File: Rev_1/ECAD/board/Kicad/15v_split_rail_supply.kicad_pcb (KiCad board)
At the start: 4 copper layers, 71.1 x 39.4 mm, 90 parts, among them Q1 NPN, Q100 IPP029N15NM6, Q101 NPN, Q102 NPN, Q103 PMOS, Q2 NPN, U1 LM3478MA, U100 LM3478MA, U2 LM358, U3 LM358, U4 SN74AHC1G02DBVR, U5 SN74AHC1G02DBVR

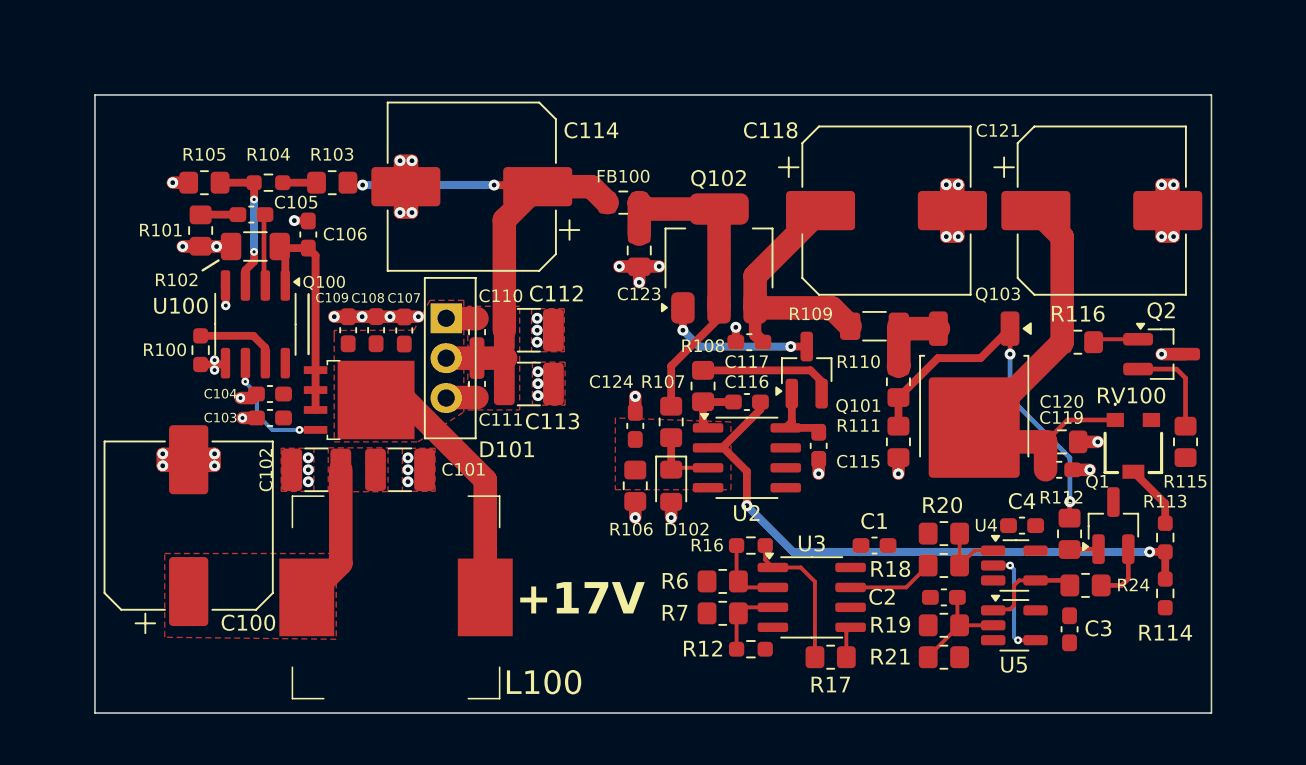
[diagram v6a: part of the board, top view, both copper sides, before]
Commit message: Added inverted buck-boost for -17V rail
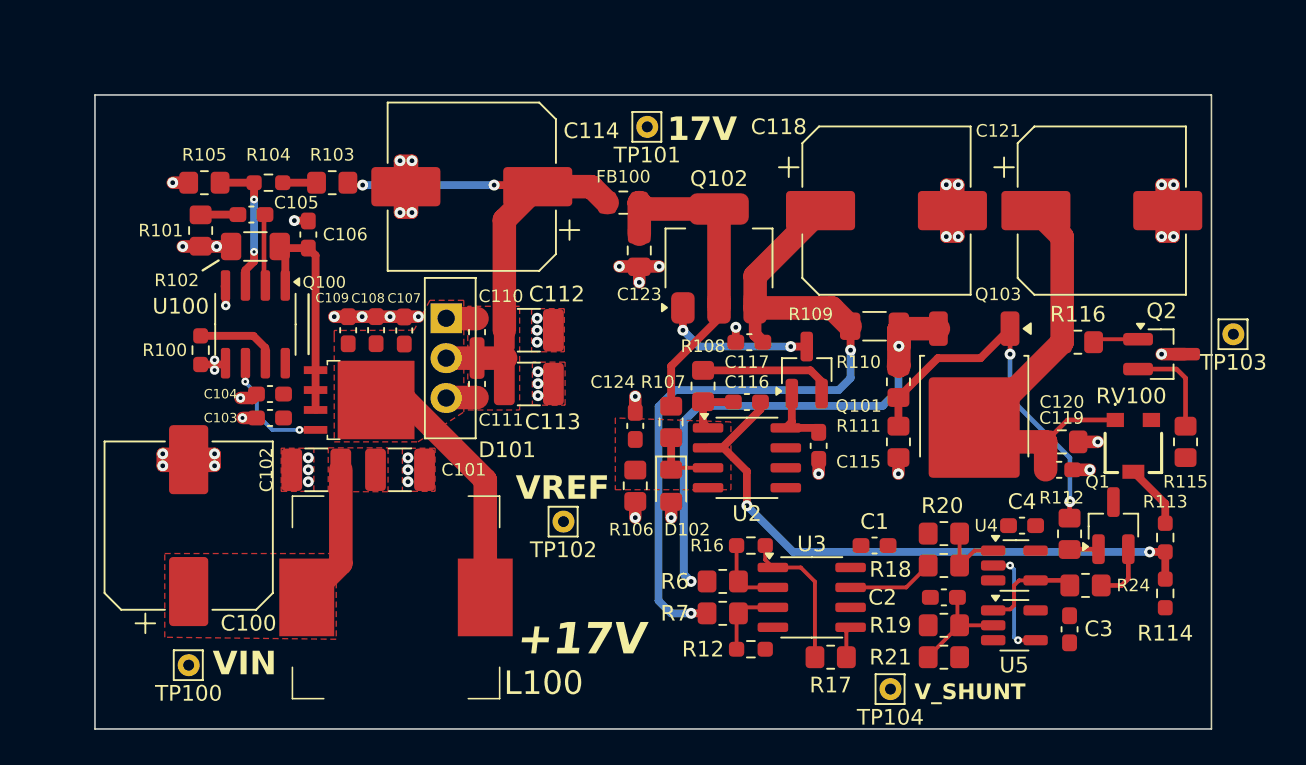
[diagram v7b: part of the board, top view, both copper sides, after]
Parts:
- added TP100: VIN, Connector_Pin:Pin_D0.7mm_L6.5mm_W1.8mm_FlatFork, F.Cu at (119.6, 104.1)
- added TP101: 17V, Connector_Pin:Pin_D0.7mm_L6.5mm_W1.8mm_FlatFork, F.Cu at (148.8, 69.8)
- added TP102: VREF, Connector_Pin:Pin_D0.7mm_L6.5mm_W1.8mm_FlatFork, F.Cu at (143.5, 95.0)
- added TP103: 15V, Connector_Pin:Pin_D0.7mm_L6.5mm_W1.8mm_FlatFork, F.Cu at (186.2, 83.1)
- added TP104: VIN, Connector_Pin:Pin_D0.7mm_L6.5mm_W1.8mm_FlatFork, F.Cu at (164.3, 105.7)
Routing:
- net /+15V DC-DC Converter/SHUNT_IN: track 16.9 -> 48.9 mm, vias 0 -> 2
- net /+15V DC-DC Converter/SHUNT_OUT: track 5.11 -> 33.6 mm, vias 0 -> 2
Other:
- board size 71.1 x 39.4 mm -> 71.1 x 40.4 mm
- board text added: "17V"
- board text added: "VIN"
- board text added: "VREF"
- board text added: "V_SHUNT"

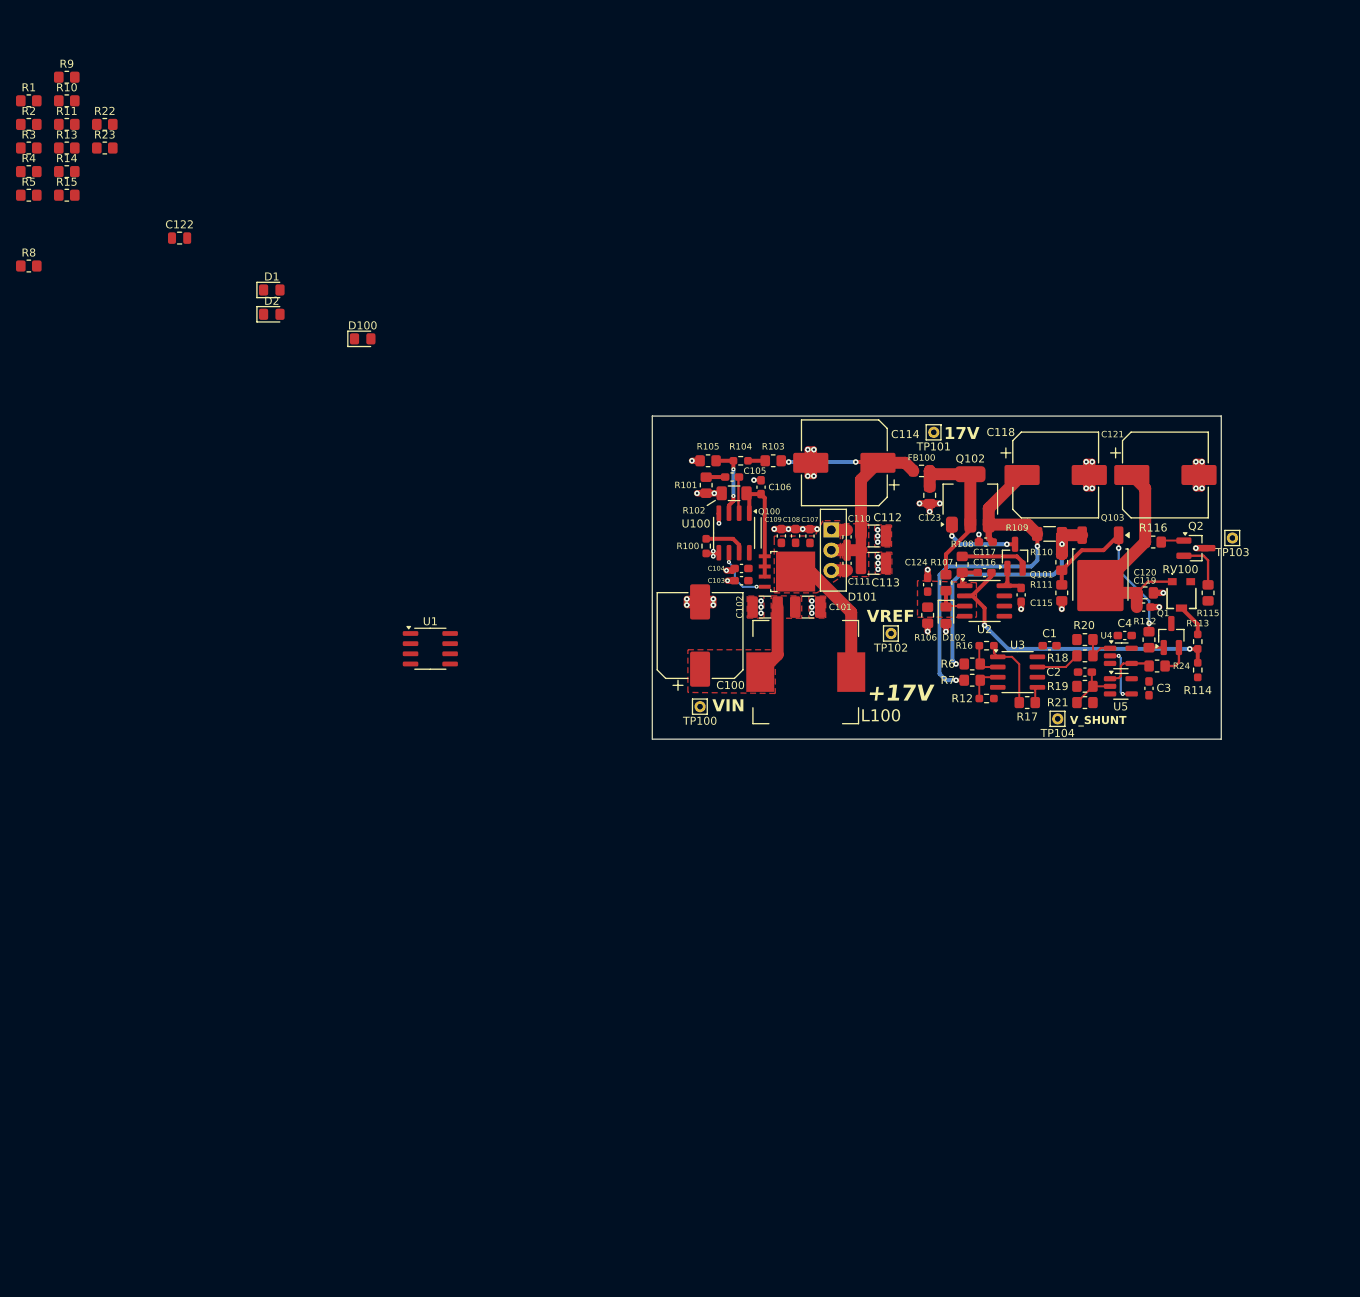
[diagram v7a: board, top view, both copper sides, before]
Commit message: Added Heatsink to Transistors
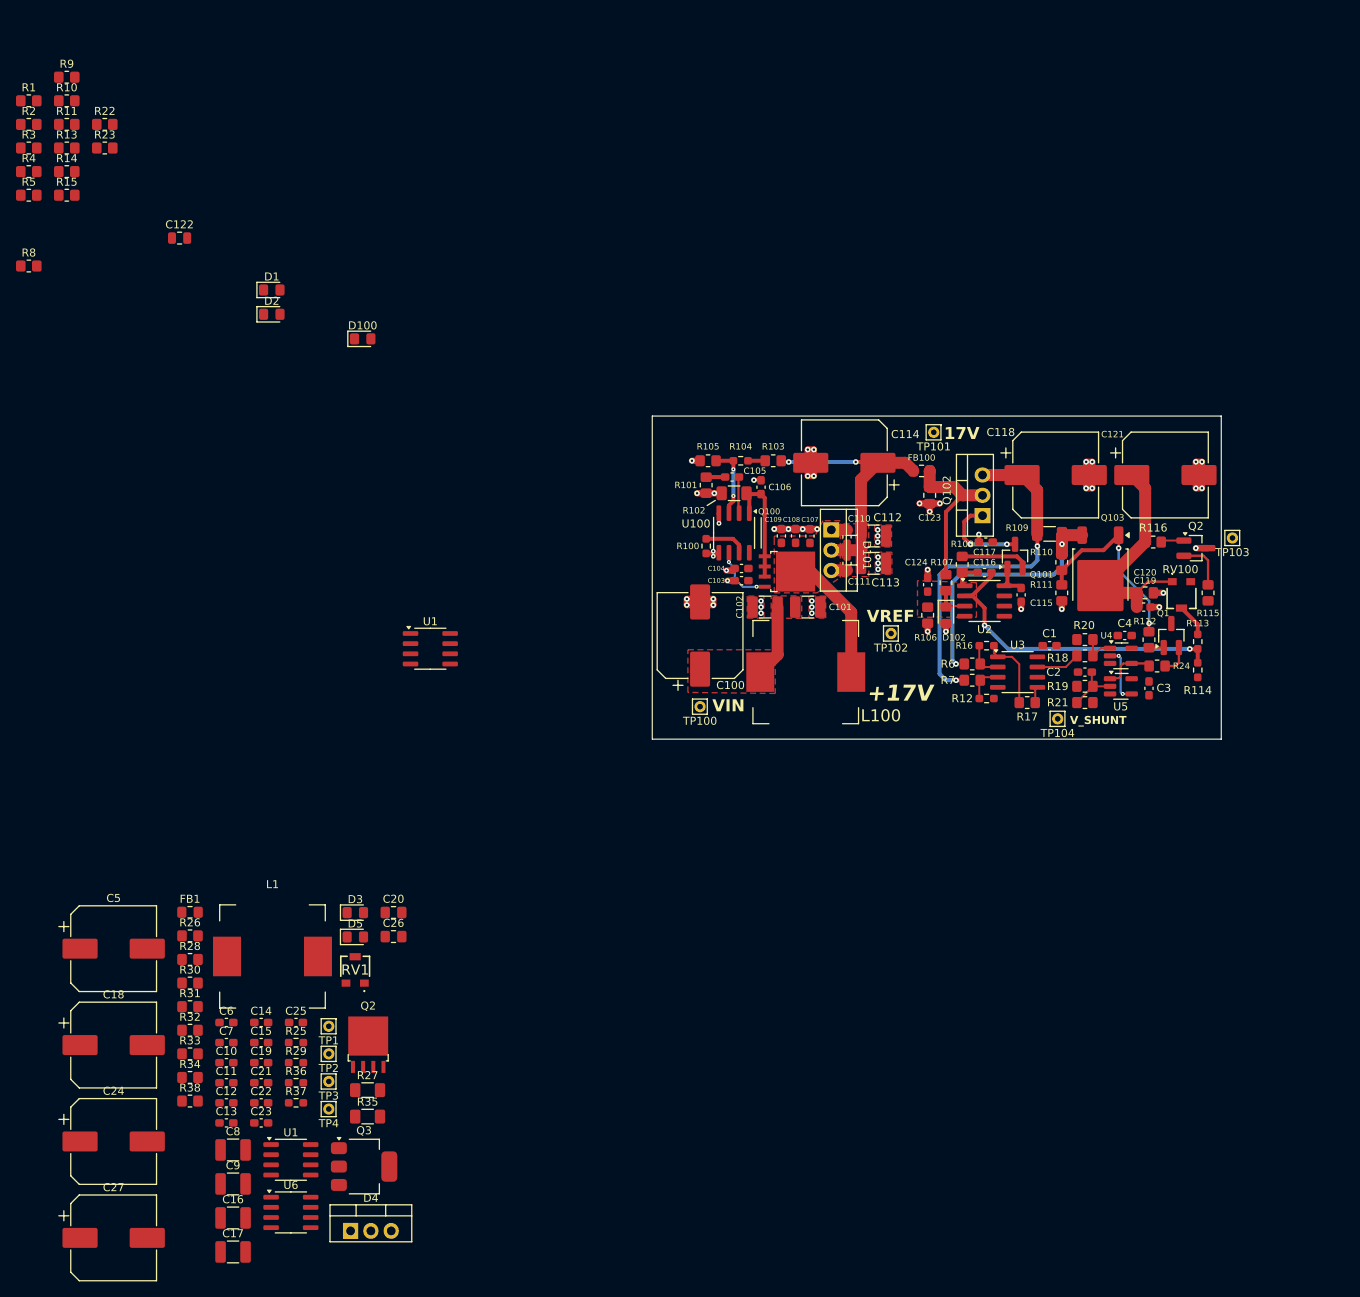
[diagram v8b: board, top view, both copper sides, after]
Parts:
- added C10: 2.2n, Capacitor_SMD:C_0603_1608Metric_Pad1.08x0.95mm_HandSolder, F.Cu at (60.4, 148.6)
- added C11: 100n, Capacitor_SMD:C_0603_1608Metric_Pad1.08x0.95mm_HandSolder, F.Cu at (60.4, 151.2)
- added C12: 100n, Capacitor_SMD:C_0603_1608Metric_Pad1.08x0.95mm_HandSolder, F.Cu at (60.4, 153.7)
- added C13: 220n, Capacitor_SMD:C_0603_1608Metric_Pad1.08x0.95mm_HandSolder, F.Cu at (60.4, 156.2)
- added C14: 1u, Capacitor_SMD:C_0603_1608Metric_Pad1.08x0.95mm_HandSolder, F.Cu at (64.8, 143.6)
- added C15: 100n, Capacitor_SMD:C_0603_1608Metric_Pad1.08x0.95mm_HandSolder, F.Cu at (64.8, 146.1)
- added C16: 47u, Capacitor_SMD:C_1210_3225Metric_Pad1.33x2.70mm_HandSolder, F.Cu at (61.3, 168.1)
- added C17: 47u, Capacitor_SMD:C_1210_3225Metric_Pad1.33x2.70mm_HandSolder, F.Cu at (61.3, 172.3)
- added C18: 220u, Capacitor_SMD:CP_Elec_10x10.5, F.Cu at (46.3, 146.4)
- added C19: 100n, Capacitor_SMD:C_0603_1608Metric_Pad1.08x0.95mm_HandSolder, F.Cu at (64.8, 148.6)
- added C20: 1u, Capacitor_SMD:C_0805_2012Metric_Pad1.18x1.45mm_HandSolder, F.Cu at (81.3, 129.9)
- added C21: 100n, Capacitor_SMD:C_0603_1608Metric_Pad1.08x0.95mm_HandSolder, F.Cu at (64.8, 151.2)
- added C22: 10p, Capacitor_SMD:C_0603_1608Metric_Pad1.08x0.95mm_HandSolder, F.Cu at (64.8, 153.7)
- added C23: 100n, Capacitor_SMD:C_0603_1608Metric_Pad1.08x0.95mm_HandSolder, F.Cu at (64.8, 156.2)
- added C24: 100u, Capacitor_SMD:CP_Elec_10x10.5, F.Cu at (46.3, 158.5)
- added C25: 1u, Capacitor_SMD:C_0603_1608Metric_Pad1.08x0.95mm_HandSolder, F.Cu at (69.1, 143.6)
- added C26: 10u, Capacitor_SMD:C_0805_2012Metric_Pad1.18x1.45mm_HandSolder, F.Cu at (81.3, 132.9)
- added C27: 220u, Capacitor_SMD:CP_Elec_10x10.5, F.Cu at (46.3, 170.5)
- added C5: 220u, Capacitor_SMD:CP_Elec_10x10.5, F.Cu at (46.3, 134.4)
- added C6: 1u, Capacitor_SMD:C_0603_1608Metric_Pad1.08x0.95mm_HandSolder, F.Cu at (60.4, 143.6)
- added C7: 100n, Capacitor_SMD:C_0603_1608Metric_Pad1.08x0.95mm_HandSolder, F.Cu at (60.4, 146.1)
- added C8: 47u, Capacitor_SMD:C_1210_3225Metric_Pad1.33x2.70mm_HandSolder, F.Cu at (61.3, 159.6)
- added C9: 47u, Capacitor_SMD:C_1210_3225Metric_Pad1.33x2.70mm_HandSolder, F.Cu at (61.3, 163.8)
- added D3: D_TVS, Diode_SMD:D_0805_2012Metric_Pad1.15x1.40mm_HandSolder, F.Cu at (76.5, 129.9)
- added D4: WNS40H100CB, Package_TO_SOT_THT:TO-220-3_Vertical, F.Cu at (75.9, 169.7)
- added D5: 5V6, Diode_SMD:D_0805_2012Metric_Pad1.15x1.40mm_HandSolder, F.Cu at (76.5, 132.9)
- added FB1: 100, Inductor_SMD:L_0805_2012Metric_Pad1.15x1.40mm_HandSolder, F.Cu at (55.9, 129.8)
- added L1: 5.6u, filip:L_IHLP5050FD_5.0x5.0mm_Shielded, F.Cu at (66.2, 135.4)
- added Q2: IPP029N15NM6, filip:TO-263-4_TabPin1-HandSoldered, F.Cu at (78.2, 146.4)
- added Q3: NPN, Package_TO_SOT_SMD:SOT-223-3_TabPin2, F.Cu at (77.6, 161.6)
- added R25: 13k, Resistor_SMD:R_0603_1608Metric_Pad0.98x0.95mm_HandSolder, F.Cu at (69.1, 146.1)
- added R26: 10k, Resistor_SMD:R_0805_2012Metric_Pad1.20x1.40mm_HandSolder, F.Cu at (55.9, 132.8)
- added R27: 20m, Resistor_SMD:R_1206_3216Metric_Pad1.30x1.75mm_HandSolder, F.Cu at (78.1, 152.1)
- added R28: 100k, Resistor_SMD:R_0805_2012Metric_Pad1.20x1.40mm_HandSolder, F.Cu at (55.9, 135.7)
- added R29: 27k, Resistor_SMD:R_0603_1608Metric_Pad0.98x0.95mm_HandSolder, F.Cu at (69.1, 148.6)
- added R30: 10k, Resistor_SMD:R_0805_2012Metric_Pad1.20x1.40mm_HandSolder, F.Cu at (55.9, 138.7)
- added R31: 100k, Resistor_SMD:R_0805_2012Metric_Pad1.20x1.40mm_HandSolder, F.Cu at (55.9, 141.6)
- added R32: 10k, Resistor_SMD:R_0805_2012Metric_Pad1.20x1.40mm_HandSolder, F.Cu at (55.9, 144.6)
- added R33: 10k, Resistor_SMD:R_0805_2012Metric_Pad1.20x1.40mm_HandSolder, F.Cu at (55.9, 147.5)
- added R34: 10, Resistor_SMD:R_0805_2012Metric_Pad1.20x1.40mm_HandSolder, F.Cu at (55.9, 150.5)
- added R35: 20m, Resistor_SMD:R_1206_3216Metric_Pad1.30x1.75mm_HandSolder, F.Cu at (78.1, 155.4)
- added R36: ?, Resistor_SMD:R_0603_1608Metric_Pad0.98x0.95mm_HandSolder, F.Cu at (69.1, 151.2)
- added R37: ?, Resistor_SMD:R_0603_1608Metric_Pad0.98x0.95mm_HandSolder, F.Cu at (69.1, 153.7)
- added R38: 100, Resistor_SMD:R_0805_2012Metric_Pad1.20x1.40mm_HandSolder, F.Cu at (55.9, 153.4)
- added RV1: 10k, filip:Potentiometer_SMD_Trimmer_PVG3_3.6x3, F.Cu at (76.5, 137.0)
- added TP1: VIN, Connector_Pin:Pin_D0.7mm_L6.5mm_W1.8mm_FlatFork, F.Cu at (73.2, 144.1)
- added TP2: -17V, Connector_Pin:Pin_D0.7mm_L6.5mm_W1.8mm_FlatFork, F.Cu at (73.2, 147.5)
- added TP3: VREF, Connector_Pin:Pin_D0.7mm_L6.5mm_W1.8mm_FlatFork, F.Cu at (73.2, 151.0)
- added TP4: -15V, Connector_Pin:Pin_D0.7mm_L6.5mm_W1.8mm_FlatFork, F.Cu at (73.2, 154.4)
- added U1: LM3478MA, Package_SO:SOIC-8_3.9x4.9mm_P1.27mm, F.Cu at (68.5, 160.8)
- added U6: LM358, Package_SO:SOIC-8_3.9x4.9mm_P1.27mm, F.Cu at (68.5, 167.4)
- D101: footprint Package_TO_SOT_THT:TO-220-3_Vertical -> filip:TO-220-3 with HeatSink
- Q102: footprint Package_TO_SOT_SMD:SOT-223-3_TabPin2 -> filip:TO-220-3 with HeatSink
- moved Q102 2.54 mm to (154.9, 80.3)
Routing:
- net /+15V DC-DC Converter/SHUNT_IN: track 48.9 -> 45.2 mm
- net Net-(Q101-E): track 9.74 -> 11.3 mm
- net +17V: track 25.6 -> 24.4 mm
